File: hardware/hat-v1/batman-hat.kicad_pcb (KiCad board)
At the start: 4 copper layers, 65 x 56.5 mm, 174 parts, among them J1 BATT pads, J2 Pi 40-pin (female, 11 mm stac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, J3 mPCIe 5.2H, J4 U.FL, J5 Tag-Connect TC2050, J6 PANEL BTN, Q1 CSD19537Q3, Q10 BSS138, Q11 Si2301CDS, Q12 BSS138, Q2 BSS138, Q3 CSD17578Q3A, Q6 BSS138, Q7 BSS138, U1 TPS26631RGER, U11 SLB9672XU2.0, U12 ATECC608C-TFLXTLS, U13 RV-3028-C7, U14 MAX-M10S-00B, U15 OPA333AIDBVR, U2 INA226AIDGSR, U3 LMR33640DDDAR, U4 LM74700QDBVRQ1, U7 TPS62933FDRLR, U8 INA226AIDGSR, U9 LTC2955ITS8-2#TRPBF

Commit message: HAT v1: routing prep for the option D placement (In1 GND zone, net classes)
Co-Authored-By: Claude Opus 5.5 <noreply@anthropic.com>
Claude-Session: https://claude.ai/code/session_01MLRuxTEmuMV82xcNLE62jW
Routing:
- added copper zone on In1.Cu, net GND
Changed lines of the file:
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@@
+    )
+  )
+  (zone (net 2) (net_name "GND") (layer "In1.Cu") (name "GND_PLANE_In1") (hatch edge 0.5)
+    (connect_pads (clearance 0.2))
+    (min_thickness 0.2) (filled_areas_thickness no)
+    (fill (thermal_gap 0.25) (thermal_bridge_width 0.35))
+    (polygon
+      (pts
+        (xy 100.3 100.3)
+        (xy 164.7 100.3)
+        (xy 164.7 156.2)
+        (xy 100.3 156.2)
+      )
     )
   )

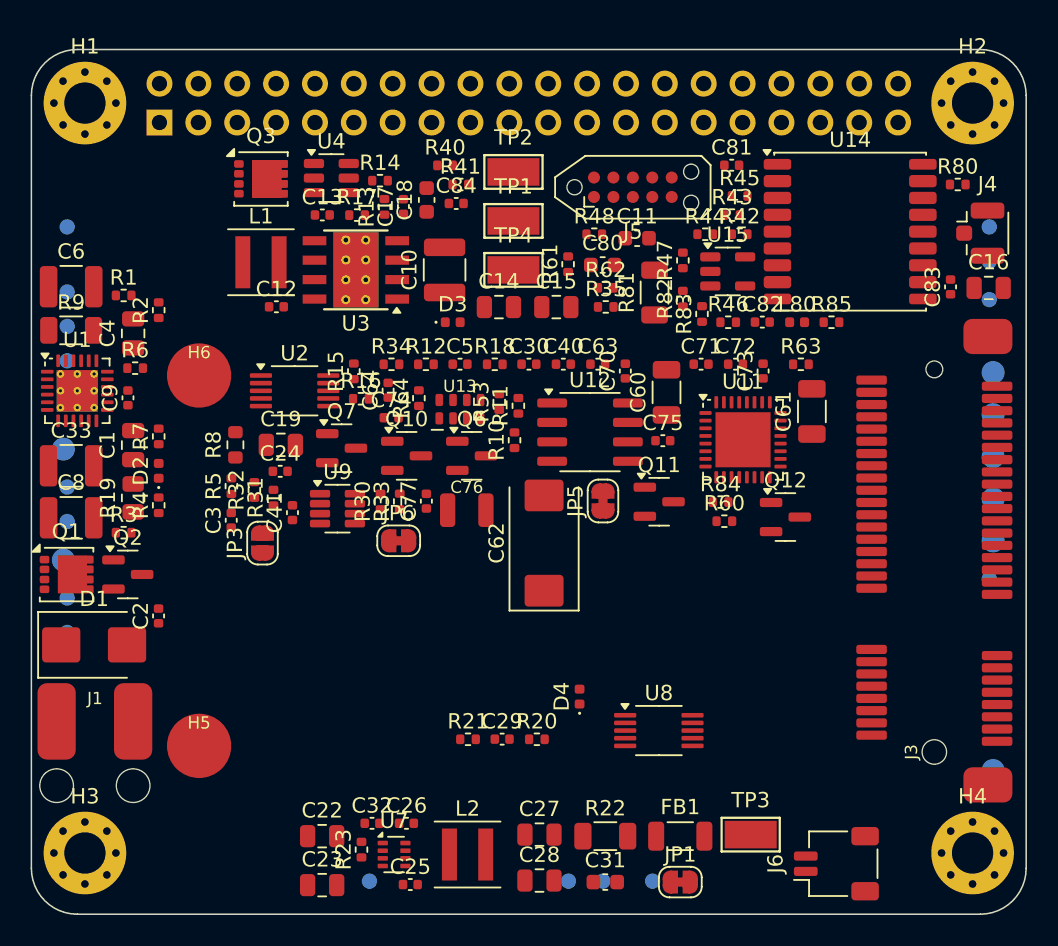
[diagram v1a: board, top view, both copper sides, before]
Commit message: HAT v1: first full routing pass (Freerouting 100 passes, GND pours); 68 unconnected pads, DRC work pending
Co-Authored-By: Claude Opus 5.5 <noreply@anthropic.com>
Claude-Session: https://claude.ai/code/session_01MLRuxTEmuMV82xcNLE62jW
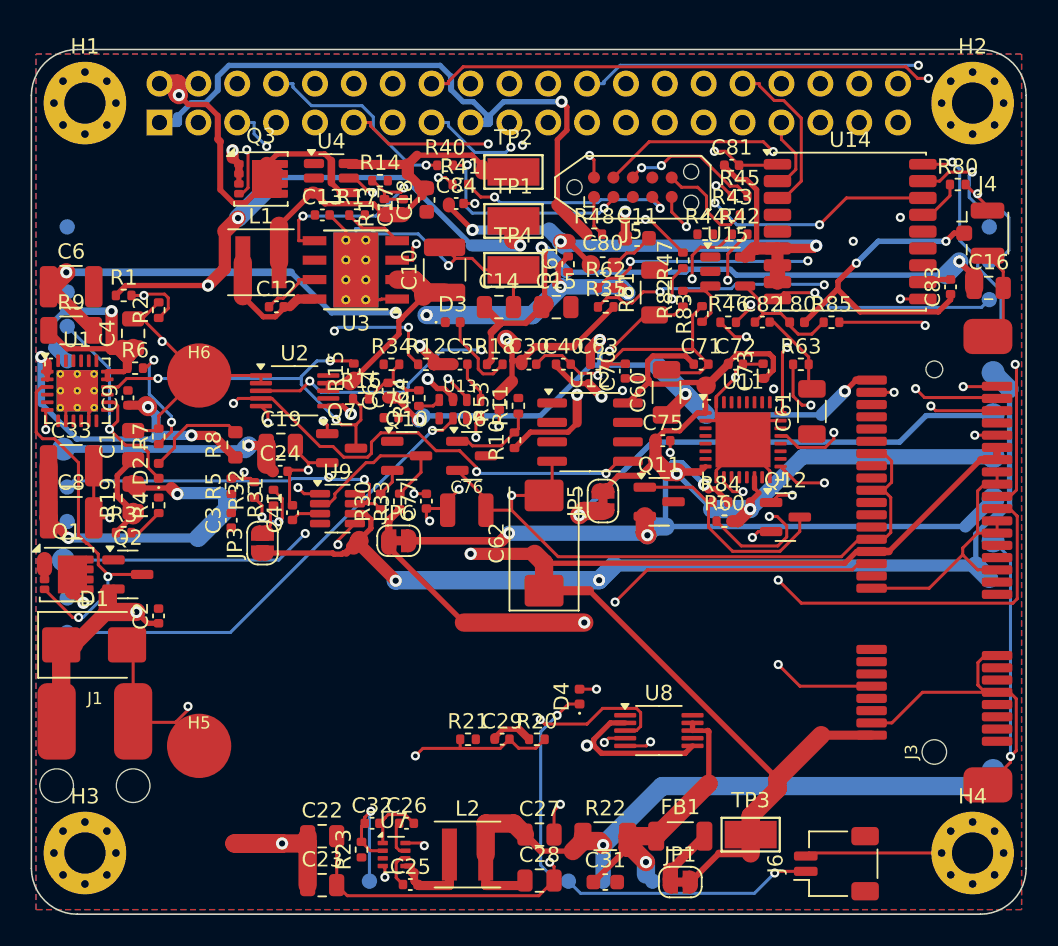
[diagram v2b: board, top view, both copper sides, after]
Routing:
- net GND: track 0.00 -> 285.8 mm, vias 0 -> 24
- net 3V3_PI: track 0.00 -> 187.3 mm, vias 0 -> 7
- net VSYS: track 0.00 -> 144.7 mm, vias 0 -> 6
- net 3V3_MPCIE: track 0.00 -> 131.2 mm, vias 0 -> 5
- net 3V3_GNSS: track 0.00 -> 112.7 mm, vias 0 -> 6
- net 5V_PI: track 0.00 -> 111.9 mm, vias 0 -> 3
- net 3V3_SEC: track 0.00 -> 99.1 mm, vias 0 -> 6
- net VBAT_RAW: track 0.00 -> 97.7 mm, vias 0 -> 5
- net 5V_BUCK: track 0.00 -> 73.0 mm, vias 0 -> 3
- net I2C1_SDA: track 0.00 -> 72.8 mm, vias 0 -> 5
- net HALOW_BUSY: track 0.00 -> 68.0 mm, vias 0 -> 2
- net HALOW_WAKE: track 0.00 -> 64.4 mm, vias 0 -> 2
- net HALOW_RESET_N: track 0.00 -> 60.7 mm, vias 0 -> 2
- net SPI0_CE0: track 0.00 -> 60.6 mm, vias 0 -> 3
- net INA_ALERT_N: track 0.00 -> 57.1 mm, vias 0 -> 5
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- added copper zone on B.Cu, net GND
- added copper zone on F.Cu, net GND
- added copper zone on In2.Cu, net GND

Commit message: HAT v1: looser placement for routability
- packer keeps a routing ring around each part: 1.0 mm for ICs / FETs / connectors,
  0.5 mm for passives (was 0.2 mm for everything)
- eFuse column moved in from the left edge; 0.45 mm track/via keep-out ring at the board edge
- H1 is a plain NPTH hole (it sits in the Pi 4 Wi-Fi keep-out)
- power-track widening now clears tracks it already widened, and skips the Wi-Fi keep-outs
- min drill 0.2 mm (QFN thermal vias); probe pads stay off IC pads that reach B.Cu

Co-Authored-By: Claude Opus 5.5 <noreply@anthropic.com>
Claude-Session: https://claude.ai/code/session_01MLRuxTEmuMV82xcNLE62jW
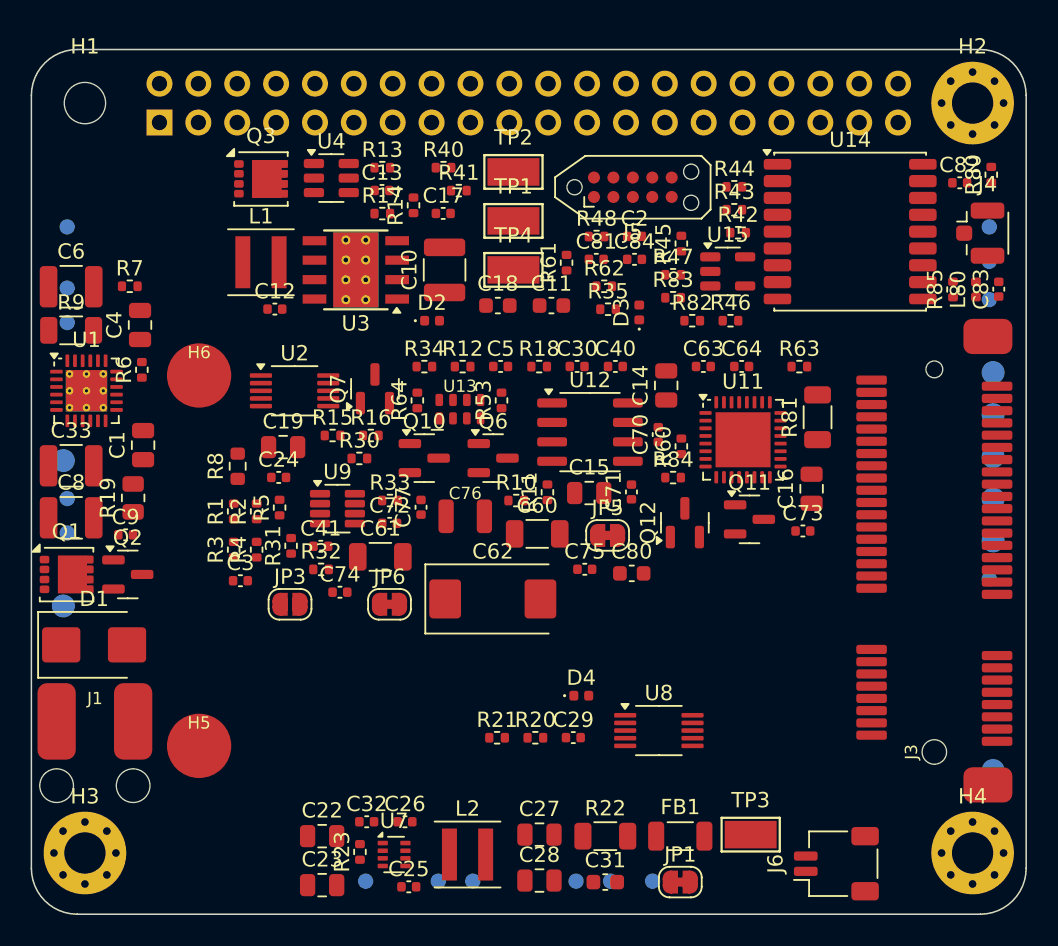
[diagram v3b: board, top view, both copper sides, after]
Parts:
- H1: footprint MountingHole_2.7mm_M2.5_Pad_Via -> MountingHole_2.7mm_M2.5
- moved C2 39.8 mm to (139.4, 112.2), turned to 0 degrees
- moved TP26 31.1 mm to (128.8, 154.3)
- moved TP25 30.5 mm to (126.6, 154.3)
- moved C61 29.8 mm to (122.8, 133.1), turned to 0 degrees
- moved C72 24.9 mm to (123.4, 131.0)
- moved C64 23.2 mm to (146.4, 120.7), turned to 0 degrees
- moved TP24 23.0 mm to (102.3, 138.8)
- moved D2 20.4 mm to (126.2, 117.7), turned to 0 degrees
- moved C80 20.2 mm to (139.2, 134.2)
- moved C16 17.5 mm to (151.0, 128.7), turned to 90 degrees
- moved R1 15.8 mm to (113.2, 130.2), turned to 90 degrees
- moved C82 15.8 mm to (160.7, 108.7)
- moved TP23 15.8 mm to (102.3, 133.8)
- moved R2 14.6 mm to (114.7, 130.2)
- moved R81 13.4 mm to (151.4, 124.0)
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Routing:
- net GND: track 285.8 -> 0.00 mm, vias 24 -> 0
- net 3V3_PI: track 187.3 -> 0.00 mm, vias 7 -> 0
- net VSYS: track 144.7 -> 0.00 mm, vias 6 -> 0
- net 3V3_MPCIE: track 131.2 -> 0.00 mm, vias 5 -> 0
- net 3V3_GNSS: track 112.7 -> 0.00 mm, vias 6 -> 0
- net 5V_PI: track 111.9 -> 0.00 mm, vias 3 -> 0
- net 3V3_SEC: track 99.1 -> 0.00 mm, vias 6 -> 0
- net VBAT_RAW: track 97.7 -> 0.00 mm, vias 5 -> 0
- net 5V_BUCK: track 73.0 -> 0.00 mm, vias 3 -> 0
- net I2C1_SDA: track 72.8 -> 0.00 mm, vias 5 -> 0
- net HALOW_BUSY: track 68.0 -> 0.00 mm, vias 2 -> 0
- net HALOW_WAKE: track 64.4 -> 0.00 mm, vias 2 -> 0
- net HALOW_RESET_N: track 60.7 -> 0.00 mm, vias 2 -> 0
- net SPI0_CE0: track 60.6 -> 0.00 mm, vias 3 -> 0
- net INA_ALERT_N: track 57.1 -> 0.00 mm, vias 5 -> 0
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- removed copper zone on B.Cu, net GND
- removed copper zone on F.Cu, net GND
- removed copper zone on In2.Cu, net GND

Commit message: HAT v1: routing pass 2 fixes (53 unconnected -> re-route)
- NexFET SON footprints: unnumbered drain leads get the drain net (were <no net> copper)
- clearance 0.127 mm (land pattern pitch on the SON gate/source pads is 0.14 mm)
- probe pads on the back avoid the Wi-Fi and GNSS keep-outs; C4 / C6 / R9 nudged

Co-Authored-By: Claude Opus 5.5 <noreply@anthropic.com>
Claude-Session: https://claude.ai/code/session_01MLRuxTEmuMV82xcNLE62jW
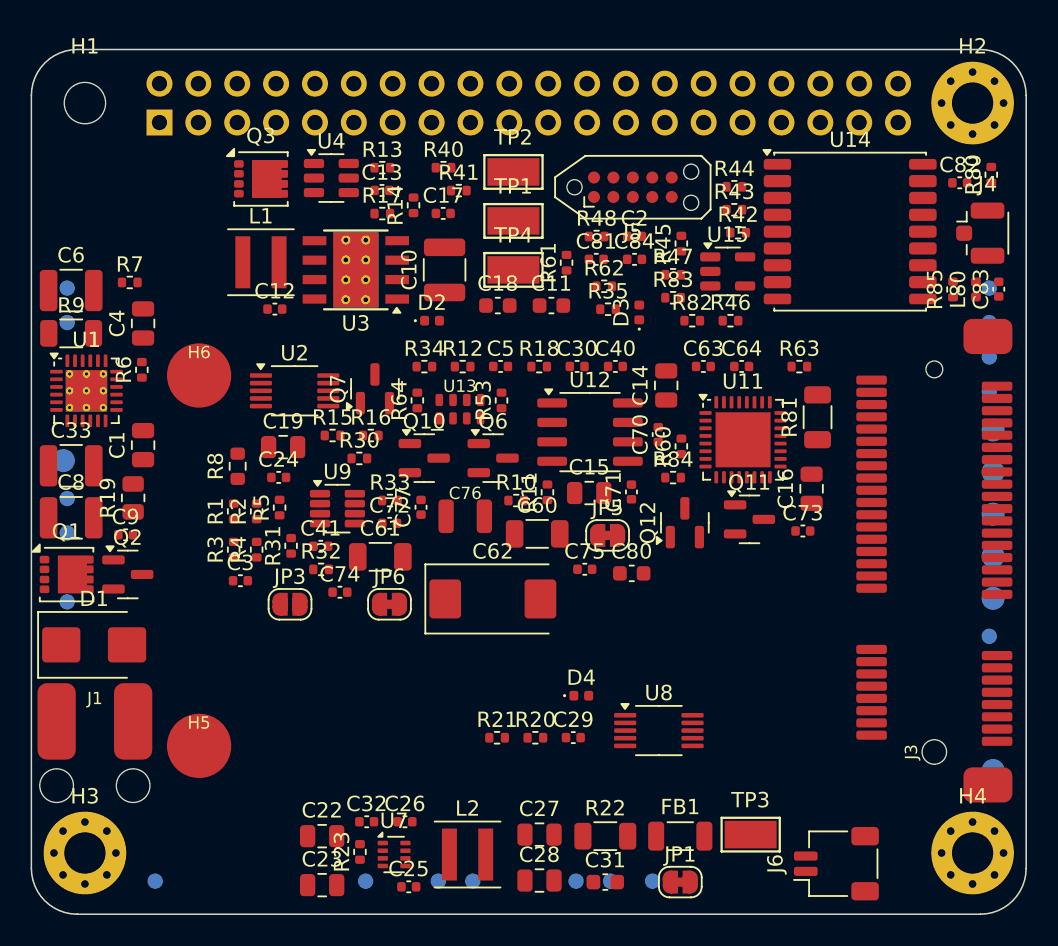
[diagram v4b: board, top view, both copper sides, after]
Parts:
- moved TP22 20.0 mm to (102.3, 131.6)
- moved TP24 16.5 mm to (108.1, 154.3)
- moved TP15 4.00 mm to (162.6, 115.6)
- moved TP16 4.00 mm to (162.6, 117.8)
- moved TP9 3.75 mm to (162.8, 130.4)
- moved TP10 3.75 mm to (162.8, 133.1)
- moved TP12 3.75 mm to (162.8, 135.9)
- moved TP13 3.75 mm to (162.6, 120.1)
- moved TP14 3.75 mm to (162.6, 122.3)
- moved TP28 3.75 mm to (162.6, 138.3)
- moved TP5 3.75 mm to (162.8, 124.9)
- moved TP8 3.75 mm to (162.8, 127.6)
- moved TP11 2.25 mm to (102.1, 138.6)
- moved TP18 2.25 mm to (102.3, 133.8)
- moved TP23 2.25 mm to (102.3, 136.1)
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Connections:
- Q1 pad : (no net) -> EF_IN
- Q3 pad : (no net) -> 5V_PI

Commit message: HAT v1: routing pass 3 - 37 unconnected (mostly GND pour islands), 0 clearance errors; incremental reroute support
Co-Authored-By: Claude Opus 5.5 <noreply@anthropic.com>
Claude-Session: https://claude.ai/code/session_01MLRuxTEmuMV82xcNLE62jW
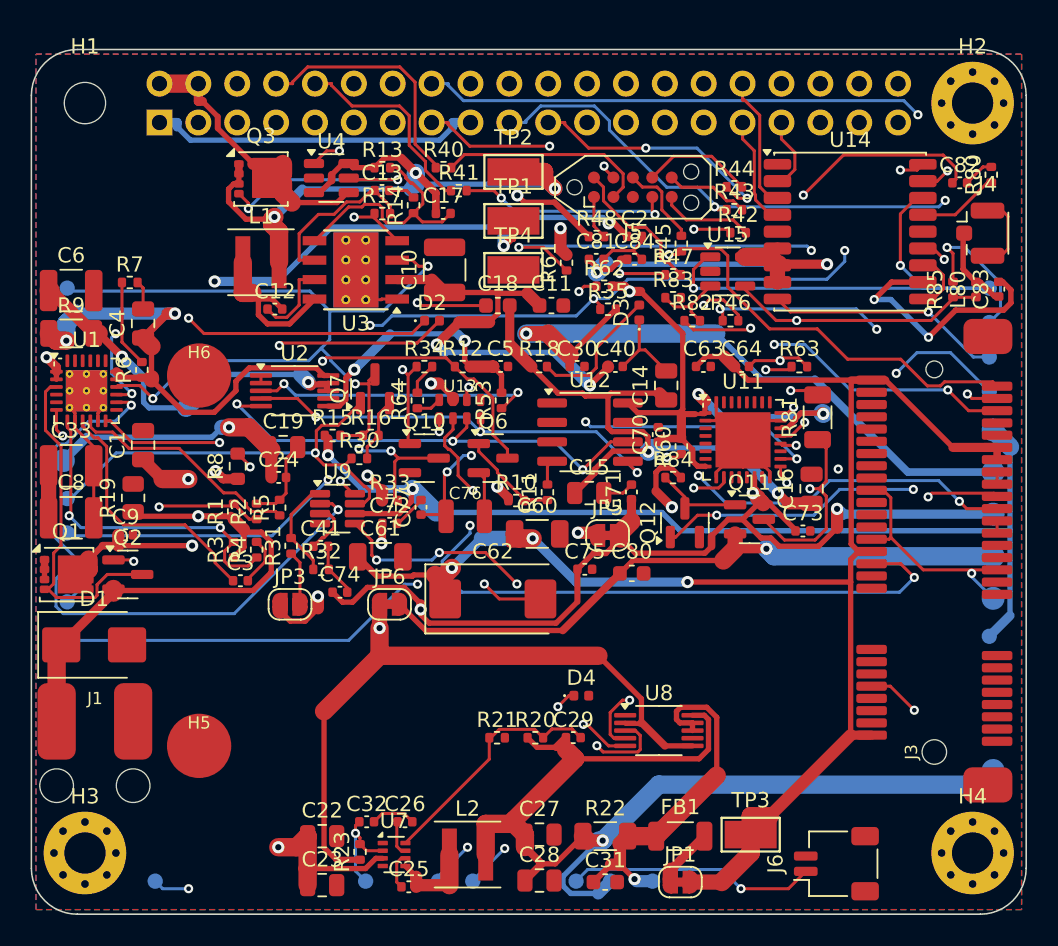
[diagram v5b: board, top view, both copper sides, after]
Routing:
- net 3V3_PI: track 0.00 -> 187.2 mm, vias 0 -> 7
- net VSYS: track 0.00 -> 150.3 mm, vias 0 -> 7
- net 3V3_SEC: track 0.00 -> 135.7 mm, vias 0 -> 9
- net VBAT_RAW: track 0.00 -> 108.9 mm, vias 0 -> 6
- net GND: track 0.00 -> 108.6 mm, vias 0 -> 3
- net 5V_BUCK: track 0.00 -> 103.3 mm, vias 0 -> 5
- net 3V3_MPCIE: track 0.00 -> 102.8 mm, vias 0 -> 3
- net 3V3_GNSS: track 0.00 -> 101.6 mm, vias 0 -> 4
- net 5V_PI: track 0.00 -> 100.6 mm, vias 0 -> 2
- net I2C1_SDA: track 0.00 -> 73.6 mm, vias 0 -> 4
- net 3V3_BUCK: track 0.00 -> 71.5 mm, vias 0 -> 1
- net INA_ALERT_N: track 0.00 -> 70.5 mm, vias 0 -> 3
- net I2C1_SCL: track 0.00 -> 70.2 mm, vias 0 -> 4
- net HALOW_RESET_N: track 0.00 -> 68.2 mm, vias 0 -> 2
- net PWR_BTN_N: track 0.00 -> 68.1 mm, vias 0 -> 5
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- added copper zone on B.Cu, net GND
- added copper zone on F.Cu, net GND
- added copper zone on In2.Cu, net GND

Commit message: HAT v1: incremental reroute + GND stitching - 19 unconnected (14 isolated GND pads, 5 signals)
- finish(replace=True) re-imports a full SES from the incremental Freerouting pass
- stitch_gnd: a via for every SMD GND pad (0.6/0.3, fallback 0.5/0.25), one per isolated pour
  fragment, then a 3 mm grid; respects hole spacing, Wi-Fi and footprint keep-outs
- pours: SMD pads solid / THT relieved, islands removed; In1 plane solid to every GND pad

Co-Authored-By: Claude Opus 5.5 <noreply@anthropic.com>
Claude-Session: https://claude.ai/code/session_01MLRuxTEmuMV82xcNLE62jW
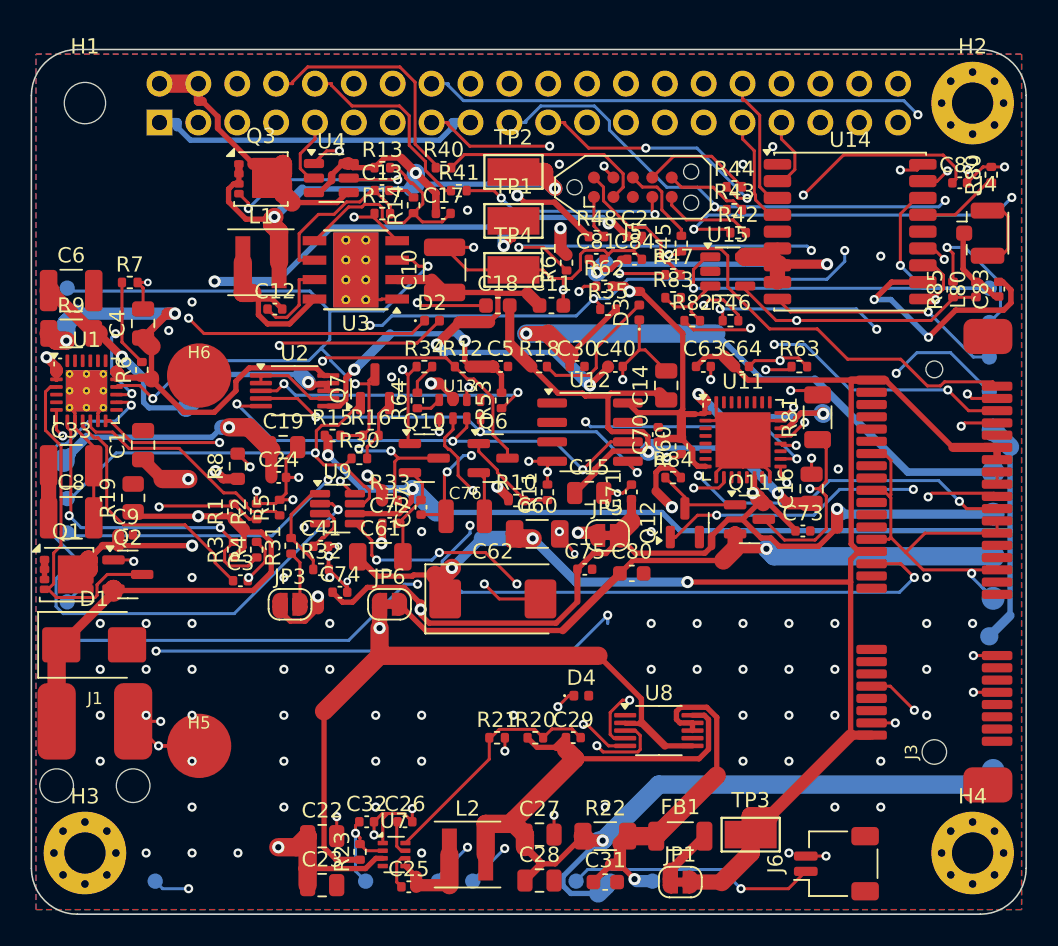
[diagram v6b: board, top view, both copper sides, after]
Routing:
- net GND: track 108.6 -> 189.4 mm, vias 3 -> 102
- net SPI0_SCLK: track 17.1 -> 57.5 mm, vias 1 -> 3
- net EF_DRV: track 1.37 -> 41.4 mm, vias 1 -> 3
- net VRTC: track 44.9 -> 49.8 mm
- net EF_UVLO: track 17.2 -> 17.9 mm
- net VCAP_5V: track 18.6 -> 19.2 mm
- net 5V_PI: track 100.6 -> 101.1 mm
- net 3V3_BUCK: track 71.5 -> 72.0 mm
- net GNSS_ANT_VREF: track 4.96 -> 5.48 mm

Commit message: HAT v1: rip-up + reroute around new GND vias - 17 unconnected (15 isolated GND pads, 2 signal)
Co-Authored-By: Claude Opus 5.5 <noreply@anthropic.com>
Claude-Session: https://claude.ai/code/session_01MLRuxTEmuMV82xcNLE62jW
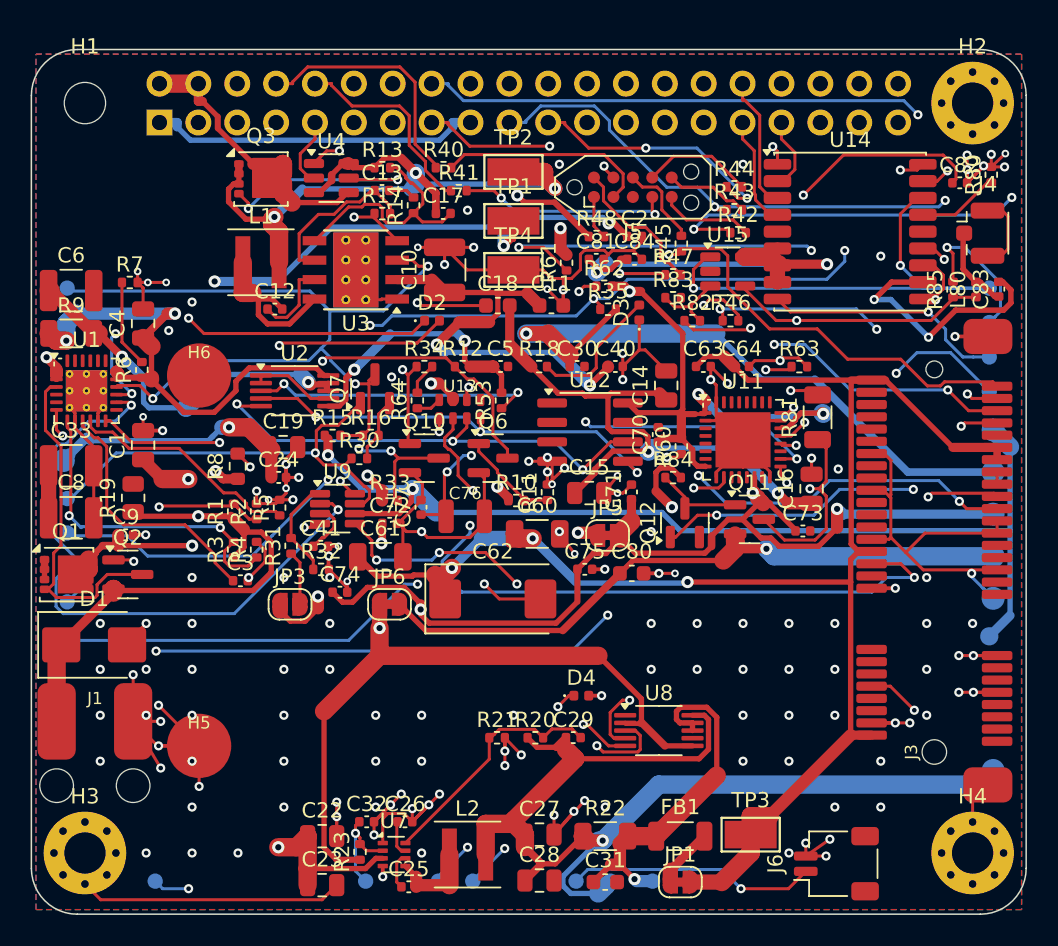
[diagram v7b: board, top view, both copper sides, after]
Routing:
- net GND: track 189.4 -> 299.5 mm, vias 102 -> 148
- net VRTC: track 49.8 -> 46.1 mm
- net EF_DRV: track 41.4 -> 38.3 mm
- net EF_IN: track 38.7 -> 39.9 mm
- net PG_5V: track 40.2 -> 41.3 mm
- net INA_ALERT_N: track 70.5 -> 71.6 mm
- net GNSS_ANT_SUP: track 28.7 -> 29.4 mm
